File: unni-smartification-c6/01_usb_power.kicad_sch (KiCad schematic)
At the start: 21 parts, among them J1 USB-C (replacement daughterbo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, J3 Conn_01x06, J4 UNNI DC / battery input - AC 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, Q2 AO3401A, Q3 AO3400A, Q4 AO3400A, U3 TPS613222ADBZ (5V), U4 TPD2E009DBZR

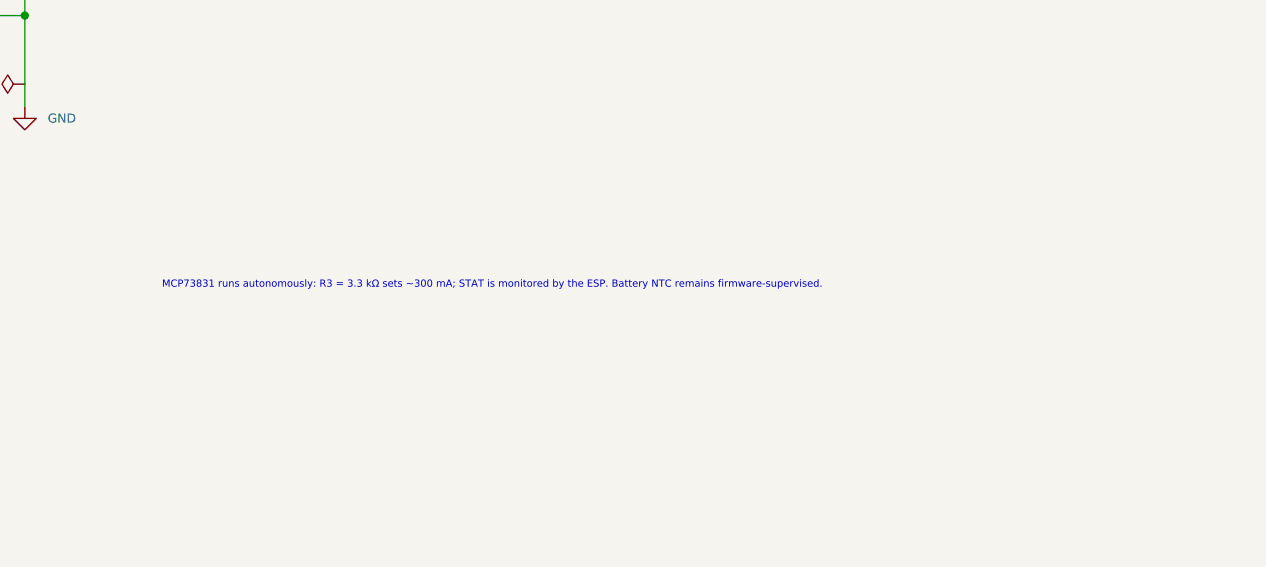
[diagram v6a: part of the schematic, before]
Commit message: Align stackup and validation with JLCPCB
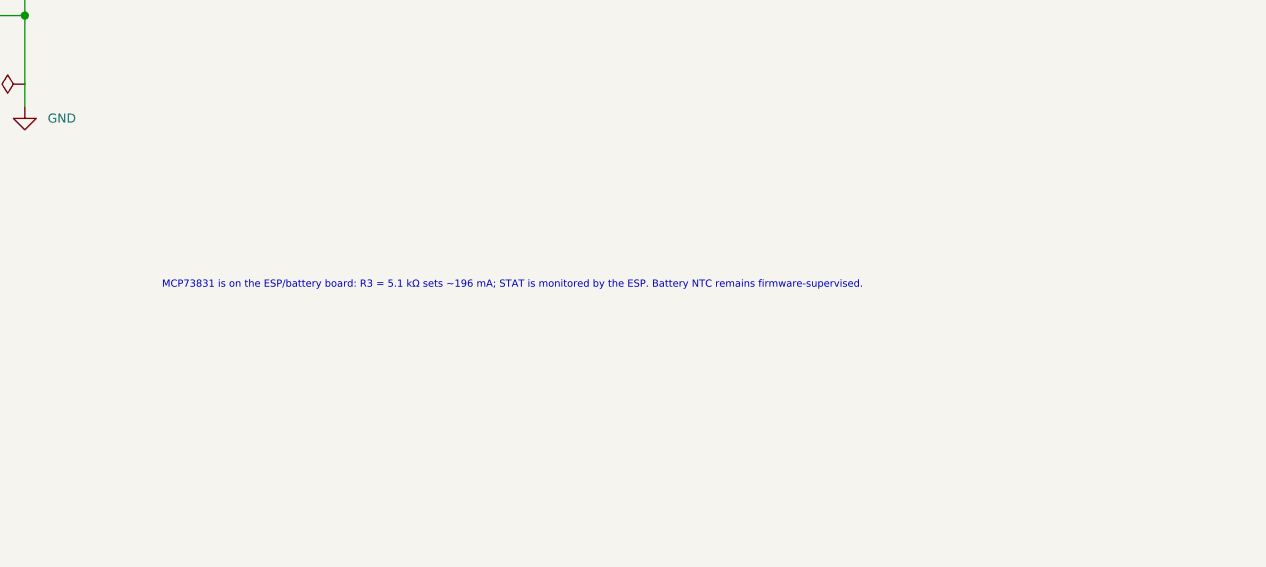
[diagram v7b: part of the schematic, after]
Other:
- note added: "MCP73831 is on the ESP/battery board: R3 = 5.1 kΩ sets ~196 mA; STAT is monitored by the ESP. Battery NTC remains firmware-supervised."
- note removed: "MCP73831 runs autonomously: R3 = 3.3 kΩ sets ~300 mA; STAT is monitored by the ESP. Battery NTC remains firmware-supervised."
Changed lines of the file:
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@@
 		(company "Unni CO2 Smartification")
 	)
-	(text "MCP73831 runs autonomously: R3 = 3.3 kΩ sets ~300 mA; STAT is monitored by the ESP. Battery NTC remains firmware-supervised."
+	(text "MCP73831 is on the ESP/battery board: R3 = 5.1 kΩ sets ~196 mA; STAT is monitored by the ESP. Battery NTC remains firmware-supervised."
 		(exclude_from_sim no)
 		(at 81.28 104.14 0)
